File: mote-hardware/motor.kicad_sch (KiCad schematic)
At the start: 16 parts, among them J7 JST_PH_B6B, J8 JST_PH_B6B, U5 DRV8833PW

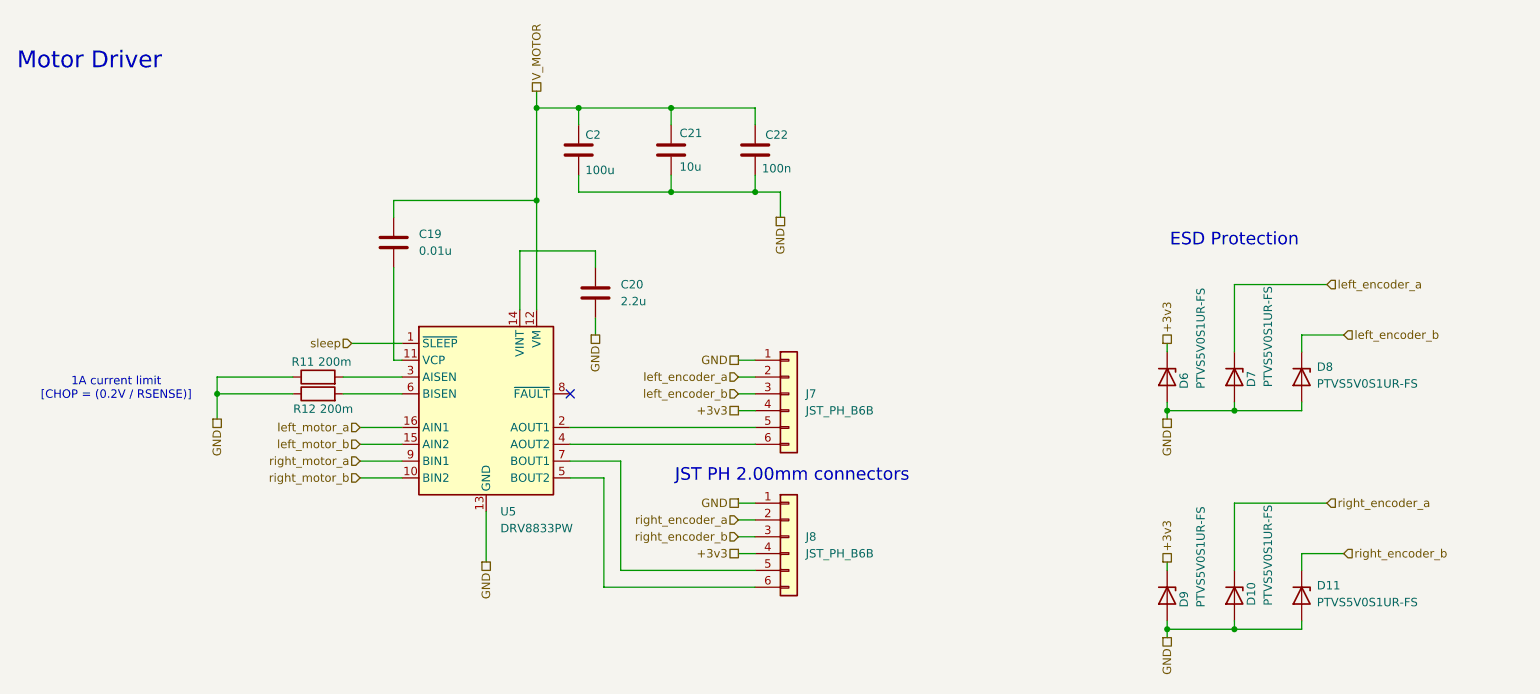
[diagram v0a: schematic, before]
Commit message: Update schematic with low cap / high speed TVS diodes
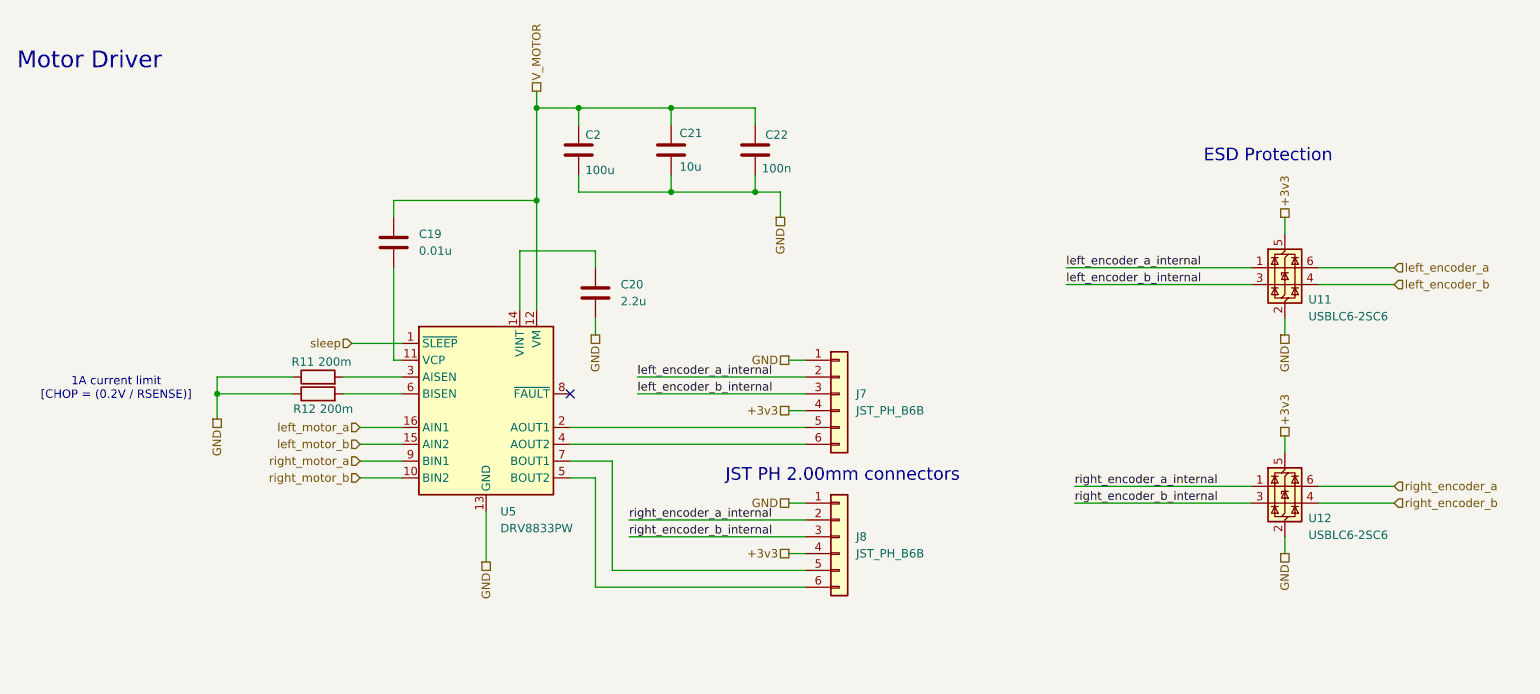
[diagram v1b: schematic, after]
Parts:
- removed D10, D11, D6, D7, D8, D9: PTVS5V0S1UR-FS, Diode_SMD:D_SOD-123, symbol Diode:PTVS5V0Z1USK
- added U11, U12: USBLC6-2SC6, Package_TO_SOT_SMD:SOT-23-6, symbol Power_Protection:USBLC6-2SC6
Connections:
- net +3v3: now also U11.5 (VBUS), U12.5 (VBUS)
- net GND: now also U11.2 (GND), U12.2 (GND)
- net left_encoder_a: now also U11.6 (I/O1); no longer J7.2 (Pin_2)
- net left_encoder_b: now also U11.4 (I/O2); no longer J7.3 (Pin_3)
- net right_encoder_a: now also U12.6 (I/O1); no longer J8.2 (Pin_2)
- net right_encoder_b: now also U12.4 (I/O2); no longer J8.3 (Pin_3)
- new net left_encoder_a_internal: J7.2 (Pin_2), U11.1 (I/O1)
- new net left_encoder_b_internal: J7.3 (Pin_3), U11.3 (I/O2)
- new net right_encoder_a_internal: J8.2 (Pin_2), U12.1 (I/O1)
- new net right_encoder_b_internal: J8.3 (Pin_3), U12.3 (I/O2)
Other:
- moved on the sheet: J7, J8

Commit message: Layout for new tvs diodes
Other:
- company: github.com/empriselab/mote-core -> github.com/empriselab/mote
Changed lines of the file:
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@@
 	(title_block
 		(title "Mote")
-		(date "2026-04-25")
-		(rev "V0.1.0")
-		(company "github.com/empriselab/mote-core")
+		(date "2026-05-25")
+		(rev "V0.2.0")
+		(company "github.com/empriselab/mote")
 	)
 	(text "JST PH 2.00mm connectors"
